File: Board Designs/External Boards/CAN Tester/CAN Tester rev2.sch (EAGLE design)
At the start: 30 parts, among them M1 Minifit-1, M2 Minifit-2, M3 Nanofit-1, M4 Nanofit-2, U1 ISOCAN, U3 TEENSY_3.2_SIMPLE, U4 CHARACTER_LCD

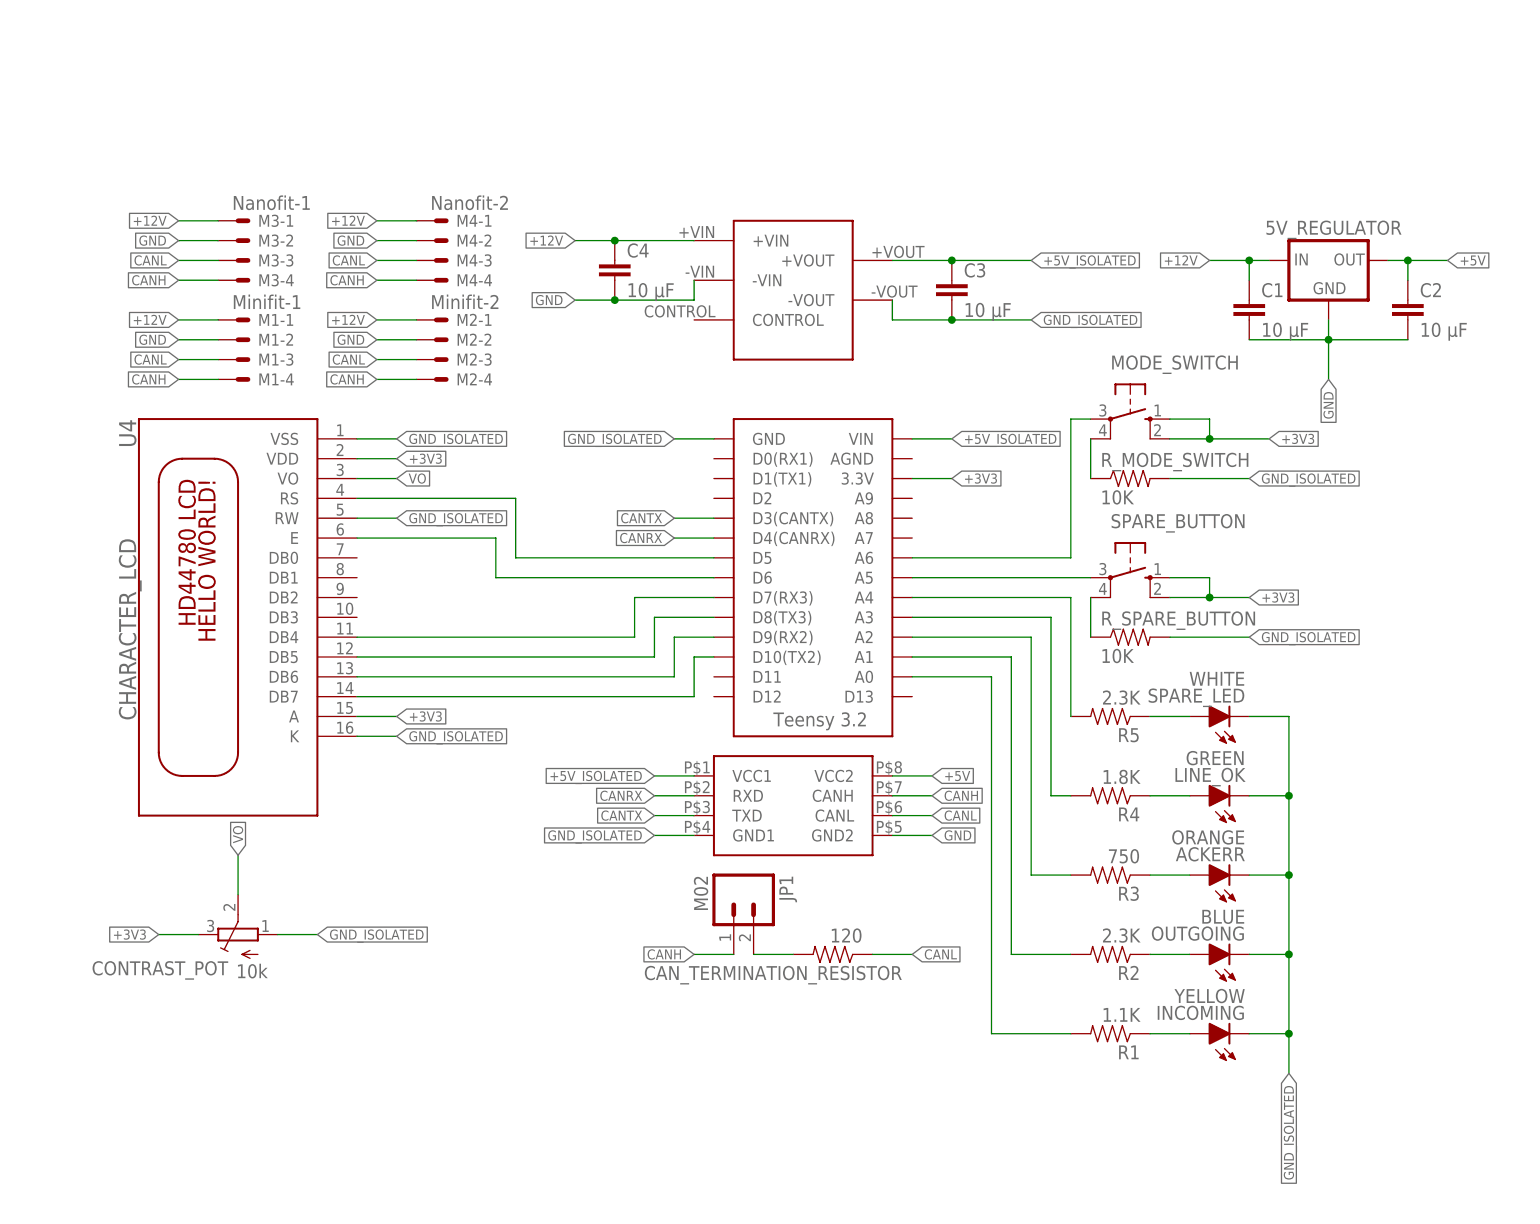
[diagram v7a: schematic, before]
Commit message: Added mounting holes and make silkscreen larger on CAN Tester
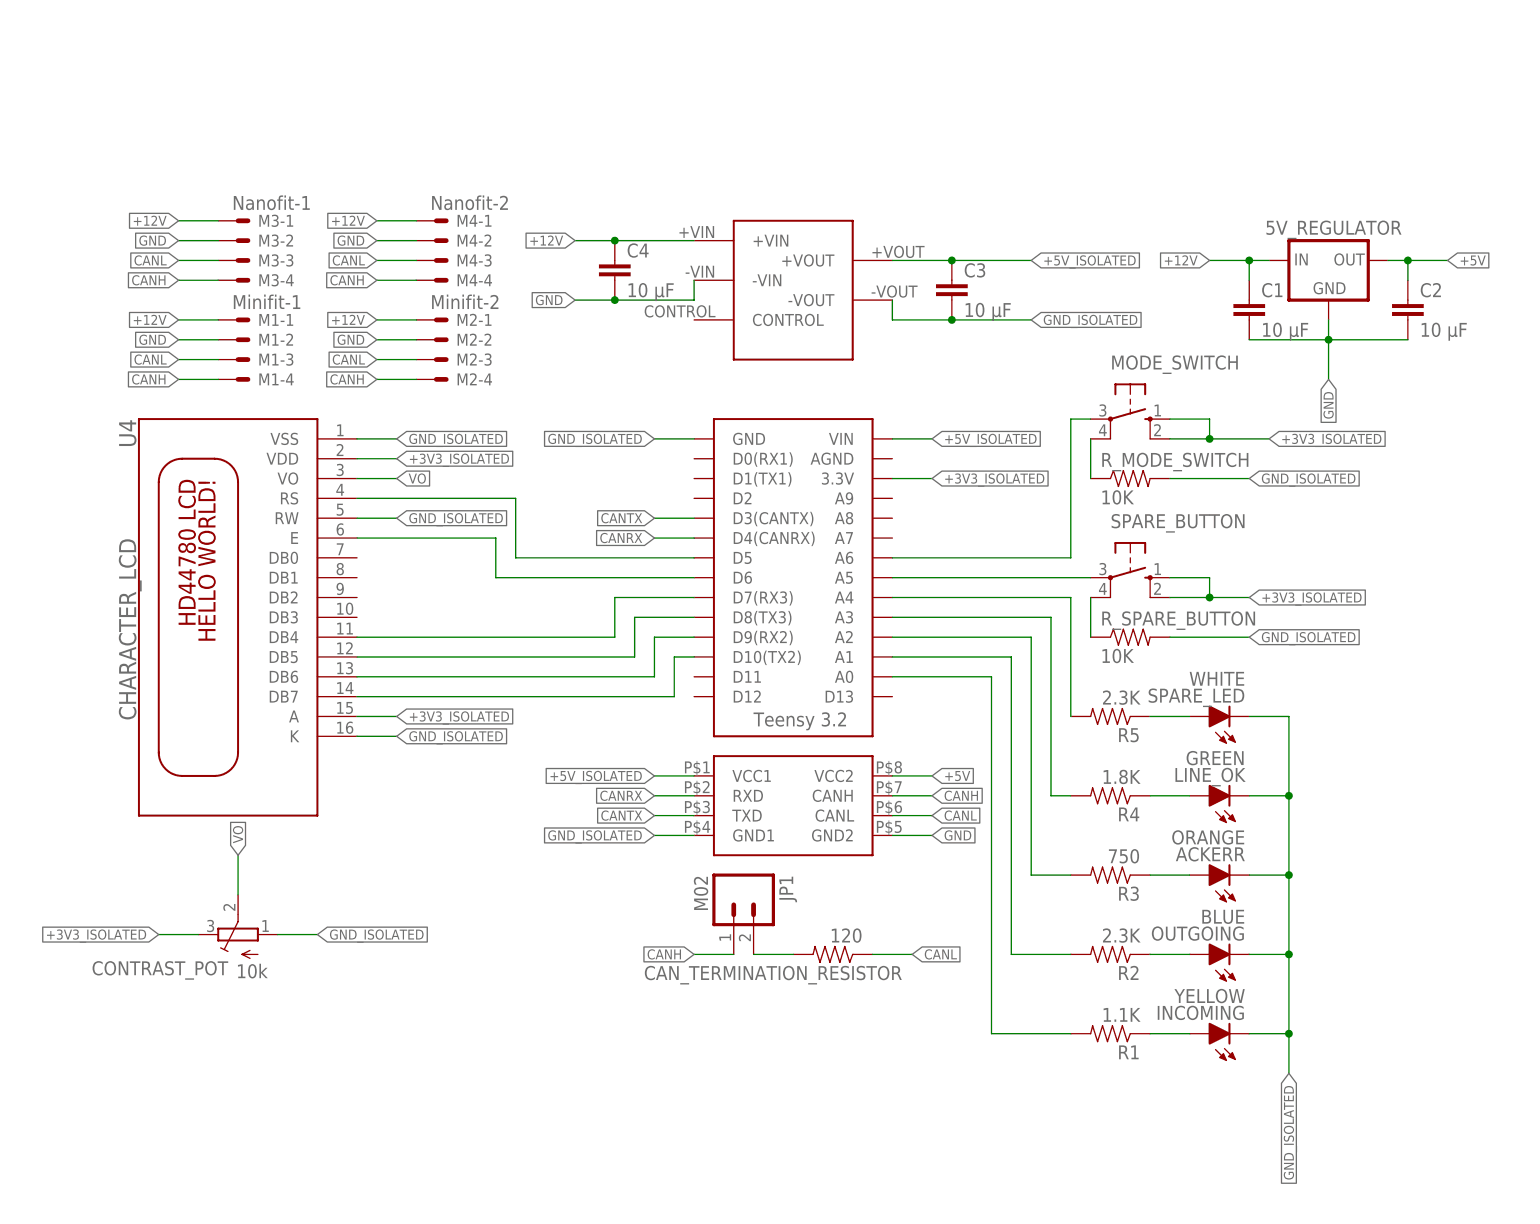
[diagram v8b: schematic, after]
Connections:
- net +3V3 renamed +3V3_ISOLATED
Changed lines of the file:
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@@
 </plain>
 <instances>
-<instance part="U3" gate="G$1" x="96.52" y="27.94" smashed="yes"/>
+<instance part="U3" gate="G$1" x="93.98" y="27.94" smashed="yes"/>
 <instance part="U1" gate="G$1" x="93.98" y="12.7" smashed="yes"/>
 <instance part="INCOMING" gate="LED" x="157.48" y="-10.16" smashed="yes" rot="R90">
@@
 <segment>
 <pinref part="U3" gate="G$1" pin="D3(CANTX)"/>
-<wire x1="93.98" y1="55.88" x2="88.9" y2="55.88" width="0.1524" layer="91"/>
-<label x="88.9" y="55.88" size="1.27" layer="95" font="vector" rot="R180" xref="yes"/>
+<wire x1="91.44" y1="55.88" x2="86.36" y2="55.88" width="0.1524" layer="91"/>
+<label x="86.36" y="55.88" size="1.27" layer="95" font="vector" rot="R180" xref="yes"/>
 </segment>
 <segment>
@@
 <segment>
 <pinref part="U3" gate="G$1" pin="D4(CANRX)"/>
-<wire x1="93.98" y1="53.34" x2="88.9" y2="53.34" width="0.1524" layer="91"/>
-<label x="88.9" y="53.34" size="1.27" layer="95" font="vector" rot="R180" xref="yes"/>
+<wire x1="91.44" y1="53.34" x2="86.36" y2="53.34" width="0.1524" layer="91"/>
+<label x="86.36" y="53.34" size="1.27" layer="95" font="vector" rot="R180" xref="yes"/>
 </segment>
 <segment>
@@
 <segment>
 <pinref part="U3" gate="G$1" pin="A0"/>
-<wire x1="119.38" y1="35.56" x2="129.54" y2="35.56" width="0.1524" layer="91"/>
+<wire x1="116.84" y1="35.56" x2="129.54" y2="35.56" width="0.1524" layer="91"/>
 <wire x1="129.54" y1="35.56" x2="129.54" y2="-10.16" width="0.1524" layer="91"/>
 <pinref part="R1" gate="G$1" pin="2"/>
@@
 <segment>
 <pinref part="U3" gate="G$1" pin="A1"/>
-<wire x1="119.38" y1="38.1" x2="132.08" y2="38.1" width="0.1524" layer="91"/>
+<wire x1="116.84" y1="38.1" x2="132.08" y2="38.1" width="0.1524" layer="91"/>
 <wire x1="132.08" y1="38.1" x2="132.08" y2="0" width="0.1524" layer="91"/>
 <pinref part="R2" gate="G$1" pin="2"/>
@@
 <segment>
 <pinref part="U3" gate="G$1" pin="A2"/>
-<wire x1="119.38" y1="40.64" x2="134.62" y2="40.64" width="0.1524" layer="91"/>
+<wire x1="116.84" y1="40.64" x2="134.62" y2="40.64" width="0.1524" layer="91"/>
 <wire x1="134.62" y1="40.64" x2="134.62" y2="10.16" width="0.1524" layer="91"/>
 <pinref part="R3" gate="G$1" pin="2"/>
@@
 <segment>
 <pinref part="U3" gate="G$1" pin="A3"/>
-<wire x1="119.38" y1="43.18" x2="137.16" y2="43.18" width="0.1524" layer="91"/>
+<wire x1="116.84" y1="43.18" x2="137.16" y2="43.18" width="0.1524" layer="91"/>
 <wire x1="137.16" y1="43.18" x2="137.16" y2="20.32" width="0.1524" layer="91"/>
 <pinref part="R4" gate="G$1" pin="2"/>
@@
 <segment>
 <pinref part="U3" gate="G$1" pin="A4"/>
-<wire x1="119.38" y1="45.72" x2="139.7" y2="45.72" width="0.1524" layer="91"/>
+<wire x1="116.84" y1="45.72" x2="139.7" y2="45.72" width="0.1524" layer="91"/>
 <pinref part="R5" gate="G$1" pin="2"/>
 <wire x1="139.7" y1="45.72" x2="139.7" y2="30.48" width="0.1524" layer="91"/>
@@
 <pinref part="U3" gate="G$1" pin="A5"/>
 <pinref part="SPARE_BUTTON" gate="1" pin="P"/>
-<wire x1="119.38" y1="48.26" x2="142.24" y2="48.26" width="0.1524" layer="91"/>
-</segment>
-</net>
-<net name="+3V3" class="0">
+<wire x1="116.84" y1="48.26" x2="142.24" y2="48.26" width="0.1524" layer="91"/>
+</segment>
+</net>
+<net name="+3V3_ISOLATED" class="0">
 <segment>
 <pinref part="U3" gate="G$1" pin="3.3V"/>
-<wire x1="119.38" y1="60.96" x2="124.46" y2="60.96" width="0.1524" layer="91"/>
-<label x="124.46" y="60.96" size="1.27" layer="95" xref="yes"/>
+<wire x1="116.84" y1="60.96" x2="121.92" y2="60.96" width="0.1524" layer="91"/>
+<label x="121.92" y="60.96" size="1.27" layer="95" xref="yes"/>
 </segment>
 <segment>
@@
 <segment>
 <pinref part="U3" gate="G$1" pin="A6"/>
-<wire x1="119.38" y1="50.8" x2="139.7" y2="50.8" width="0.1524" layer="91"/>
+<wire x1="116.84" y1="50.8" x2="139.7" y2="50.8" width="0.1524" layer="91"/>
 <wire x1="139.7" y1="50.8" x2="139.7" y2="68.58" width="0.1524" layer="91"/>
 <wire x1="139.7" y1="68.58" x2="142.24" y2="68.58" width="0.1524" layer="91"/>
@@
 <wire x1="68.58" y1="58.42" x2="68.58" y2="50.8" width="0.1524" layer="91"/>
 <pinref part="U3" gate="G$1" pin="D5"/>
-<wire x1="68.58" y1="50.8" x2="93.98" y2="50.8" width="0.1524" layer="91"/>
+<wire x1="68.58" y1="50.8" x2="91.44" y2="50.8" width="0.1524" layer="91"/>
 </segment>
 </net>
@@
 <wire x1="66.04" y1="53.34" x2="66.04" y2="48.26" width="0.1524" layer="91"/>
 <pinref part="U3" gate="G$1" pin="D6"/>
-<wire x1="66.04" y1="48.26" x2="93.98" y2="48.26" width="0.1524" layer="91"/>
+<wire x1="66.04" y1="48.26" x2="91.44" y2="48.26" width="0.1524" layer="91"/>
 </segment>
 </net>
@@
 <segment>
 <pinref part="U4" gate="G$1" pin="DB4"/>
-<wire x1="48.26" y1="40.64" x2="83.82" y2="40.64" width="0.1524" layer="91"/>
-<wire x1="83.82" y1="40.64" x2="83.82" y2="45.72" width="0.1524" layer="91"/>
+<wire x1="48.26" y1="40.64" x2="81.28" y2="40.64" width="0.1524" layer="91"/>
+<wire x1="81.28" y1="40.64" x2="81.28" y2="45.72" width="0.1524" layer="91"/>
 <pinref part="U3" gate="G$1" pin="D7(RX3)"/>
-<wire x1="83.82" y1="45.72" x2="93.98" y2="45.72" width="0.1524" layer="91"/>
+<wire x1="81.28" y1="45.72" x2="91.44" y2="45.72" width="0.1524" layer="91"/>
 </segment>
 </net>
@@
 <segment>
 <pinref part="U4" gate="G$1" pin="DB5"/>
-<wire x1="48.26" y1="38.1" x2="86.36" y2="38.1" width="0.1524" layer="91"/>
-<wire x1="86.36" y1="38.1" x2="86.36" y2="43.18" width="0.1524" layer="91"/>
+<wire x1="48.26" y1="38.1" x2="83.82" y2="38.1" width="0.1524" layer="91"/>
+<wire x1="83.82" y1="38.1" x2="83.82" y2="43.18" width="0.1524" layer="91"/>
 <pinref part="U3" gate="G$1" pin="D8(TX3)"/>
-<wire x1="86.36" y1="43.18" x2="93.98" y2="43.18" width="0.1524" layer="91"/>
+<wire x1="83.82" y1="43.18" x2="91.44" y2="43.18" width="0.1524" layer="91"/>
 </segment>
 </net>
@@
 <segment>
 <pinref part="U4" gate="G$1" pin="DB6"/>
-<wire x1="48.26" y1="35.56" x2="88.9" y2="35.56" width="0.1524" layer="91"/>
-<wire x1="88.9" y1="35.56" x2="88.9" y2="40.64" width="0.1524" layer="91"/>
+<wire x1="48.26" y1="35.56" x2="86.36" y2="35.56" width="0.1524" layer="91"/>
+<wire x1="86.36" y1="35.56" x2="86.36" y2="40.64" width="0.1524" layer="91"/>
 <pinref part="U3" gate="G$1" pin="D9(RX2)"/>
-<wire x1="88.9" y1="40.64" x2="93.98" y2="40.64" width="0.1524" layer="91"/>
+<wire x1="86.36" y1="40.64" x2="91.44" y2="40.64" width="0.1524" layer="91"/>
 </segment>
 </net>
@@
 <segment>
 <pinref part="U4" gate="G$1" pin="DB7"/>
-<wire x1="48.26" y1="33.02" x2="91.44" y2="33.02" width="0.1524" layer="91"/>
-<wire x1="91.44" y1="33.02" x2="91.44" y2="38.1" width="0.1524" layer="91"/>
+<wire x1="48.26" y1="33.02" x2="88.9" y2="33.02" width="0.1524" layer="91"/>
+<wire x1="88.9" y1="33.02" x2="88.9" y2="38.1" width="0.1524" layer="91"/>
 <pinref part="U3" gate="G$1" pin="D10(TX2)"/>
-<wire x1="91.44" y1="38.1" x2="93.98" y2="38.1" width="0.1524" layer="91"/>
+<wire x1="88.9" y1="38.1" x2="91.44" y2="38.1" width="0.1524" layer="91"/>
 </segment>
 </net>
@@
 <segment>
 <pinref part="U3" gate="G$1" pin="VIN"/>
-<wire x1="119.38" y1="66.04" x2="124.46" y2="66.04" width="0.1524" layer="91"/>
-<label x="124.46" y="66.04" size="1.27" layer="95" xref="yes"/>
+<wire x1="116.84" y1="66.04" x2="121.92" y2="66.04" width="0.1524" layer="91"/>
+<label x="121.92" y="66.04" size="1.27" layer="95" xref="yes"/>
 </segment>
 <segment>
@@
 <segment>
 <pinref part="U3" gate="G$1" pin="GND"/>
-<wire x1="93.98" y1="66.04" x2="88.9" y2="66.04" width="0.1524" layer="91"/>
-<label x="88.9" y="66.04" size="1.27" layer="95" rot="R180" xref="yes"/>
-</segment>
-<segment>
+<wire x1="91.44" y1="66.04" x2="86.36" y2="66.04" width="0.1524" layer="91"/>
+<label x="86.36" y="66.04" size="1.27" layer="95" rot="R180" xref="yes"/>
+</segment>
+<segment>
